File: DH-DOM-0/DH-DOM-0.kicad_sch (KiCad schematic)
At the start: 30 parts, among them J1 USB_C_Receptacle_USB2.0_14P, SW1 RST, SW2 BOOT, U1 MMC5983MA, U2 LSM6DSOXTR, U3 ESP32-S3-WROOM-1, U4 NCP1117-3.3_SOT223, U5 TVS1400DRV, U7 ST7789

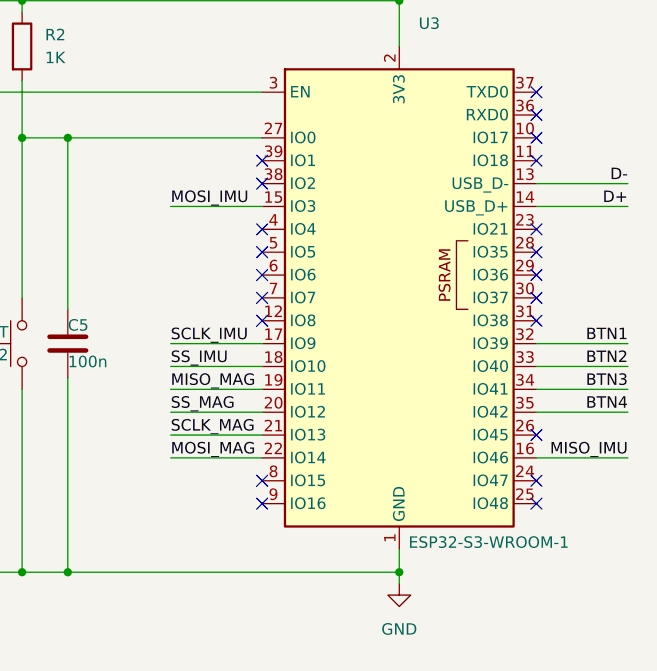
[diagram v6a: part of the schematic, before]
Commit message: edit
pcb almost done, last decoupling capacitors and screen routing left. also needs drc check
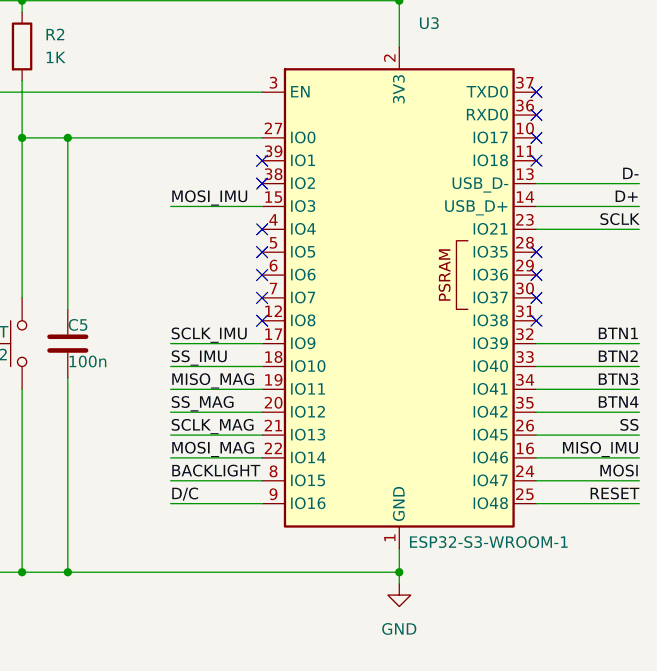
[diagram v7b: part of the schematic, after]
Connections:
- net BACKLIGHT: now also U3.8 (IO15)
- net D/C: now also U3.9 (IO16)
- net MOSI: now also U3.24 (IO47)
- net RESET: now also U3.25 (IO48)
- net SCLK: now also U3.23 (IO21)
- net SS: now also U3.26 (IO45)
- no-connect marks 27 -> 21
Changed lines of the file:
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@@
-	)
-	(no_connect
-		(at 154.94 116.84)
-	)
-	(no_connect
-		(at 185.42 116.84)
 	)
 	(no_connect
@@
 	)
 	(no_connect
-		(at 185.42 86.36)
-	)
-	(no_connect
 		(at 97.79 30.48)
 	)
@@
 	)
 	(no_connect
-		(at 185.42 109.22)
-	)
-	(no_connect
 		(at 154.94 93.98)
 	)
@@
 	)
 	(no_connect
-		(at 185.42 114.3)
-	)
-	(no_connect
 		(at 154.94 81.28)
-	)
-	(no_connect
-		(at 154.94 114.3)
 	)
 	(no_connect
@@
 	(wire
 		(pts
+			(xy 185.42 106.68) (xy 196.85 106.68)
+		)
+		(stroke
+			(width 0)
+			(type default)
+		)
+	)
+	(wire
+		(pts
 			(xy 41.91 45.72) (xy 41.91 49.53)
 		)
@@
 	(wire
 		(pts
-			(xy 185.42 101.6) (xy 195.58 101.6)
-		)
-		(stroke
-			(width 0)
-			(type default)
-		)
-	)
-	(wire
-		(pts
 			(xy 39.37 157.48) (xy 43.18 157.48)
 		)
@@
 	(wire
 		(pts
-			(xy 185.42 111.76) (xy 195.58 111.76)
-		)
-		(stroke
-			(width 0)
-			(type default)
-		)
-	)
-	(wire
-		(pts
-			(xy 185.42 83.82) (xy 195.58 83.82)
+			(xy 185.42 116.84) (xy 196.85 116.84)
 		)
 		(stroke
@@
 	(wire
 		(pts
+			(xy 185.42 99.06) (xy 196.85 99.06)
+		)
+		(stroke
+			(width 0)
+			(type default)
+		)
+	)
+	(wire
+		(pts
 			(xy 107.95 49.53) (xy 113.03 49.53)
 		)
@@
 	(wire
 		(pts
-			(xy 185.42 99.06) (xy 195.58 99.06)
-		)
-		(stroke
-			(width 0)
-			(type default)
-		)
-	)
-	(wire
-		(pts
 			(xy 63.5 68.58) (xy 69.85 68.58)
 		)
@@
 	(wire
 		(pts
+			(xy 185.42 104.14) (xy 196.85 104.14)
+		)
+		(stroke
+			(width 0)
+			(type default)
+		)
+	)
+	(wire
+		(pts
 			(xy 128.27 69.85) (xy 128.27 76.2)
 		)
@@
 	(wire
 		(pts
-			(xy 185.42 104.14) (xy 195.58 104.14)
-		)
-		(stroke
-			(width 0)
-			(type default)
-		)
-	)
-	(wire
-		(pts
 			(xy 39.37 19.05) (xy 41.91 19.05)
 		)
@@
 	(wire
 		(pts
+			(xy 185.42 81.28) (xy 196.85 81.28)
+		)
+		(stroke
+			(width 0)
+			(type default)
+		)
+	)
+	(wire
+		(pts
 			(xy 128.27 104.14) (xy 128.27 124.46)
 		)
@@
 	(wire
 		(pts
+			(xy 185.42 83.82) (xy 196.85 83.82)
+		)
+		(stroke
+			(width 0)
+			(type default)
+		)
+	)
+	(wire
+		(pts
 			(xy 113.03 16.51) (xy 113.03 19.05)
 		)
@@
 	(wire
 		(pts
-			(xy 185.42 106.68) (xy 195.58 106.68)
-		)
-		(stroke
-			(width 0)
-			(type default)
-		)
-	)
-	(wire
-		(pts
 			(xy 87.63 106.68) (xy 91.44 106.68)
 		)
@@
 	(wire
 		(pts
+			(xy 185.42 86.36) (xy 196.85 86.36)
+		)
+		(stroke
+			(width 0)
+			(type default)
+		)
+	)
+	(wire
+		(pts
 			(xy 15.24 133.35) (xy 15.24 138.43)
 		)
@@
 	(wire
 		(pts
+			(xy 185.42 109.22) (xy 196.85 109.22)
+		)
+		(stroke
+			(width 0)
+			(type default)
+		)
+	)
+	(wire
+		(pts
 			(xy 101.6 19.05) (xy 101.6 30.48)
 		)
@@
 	(wire
 		(pts
+			(xy 144.78 116.84) (xy 154.94 116.84)
+		)
+		(stroke
+			(width 0)
+			(type default)
+		)
+	)
+	(wire
+		(pts
 			(xy 81.28 45.72) (xy 81.28 49.53)
 		)
@@
 	(wire
 		(pts
+			(xy 144.78 114.3) (xy 154.94 114.3)
+		)
+		(stroke
+			(width 0)
+			(type default)
+		)
+	)
+	(wire
+		(pts
+			(xy 185.42 111.76) (xy 196.85 111.76)
+		)
+		(stroke
+			(width 0)
+			(type default)
+		)
+	)
+	(wire
+		(pts
 			(xy 73.66 157.48) (xy 77.47 157.48)
 		)
@@
 	(wire
 		(pts
-			(xy 185.42 81.28) (xy 195.58 81.28)
-		)
-		(stroke
-			(width 0)
-			(type default)
-		)
-	)
-	(wire
-		(pts
 			(xy 91.44 106.68) (xy 91.44 107.95)
 		)
@@
 	(wire
 		(pts
+			(xy 185.42 101.6) (xy 196.85 101.6)
+		)
+		(stroke
+			(width 0)
+			(type default)
+		)
+	)
+	(wire
+		(pts
 			(xy 110.49 60.96) (xy 128.27 60.96)
 		)
@@
 	(wire
 		(pts
+			(xy 185.42 114.3) (xy 196.85 114.3)
+		)
+		(stroke
+			(width 0)
+			(type default)
+		)
+	)
+	(wire
+		(pts
 			(xy 45.72 73.66) (xy 45.72 76.2)
 		)
@@
 	)
 	(label "D+"
-		(at 195.58 83.82 180)
+		(at 196.85 83.82 180)
 		(effects
 			(font
@@
 		)
 	)
+	(label "SCLK"
+		(at 196.85 86.36 180)
+		(effects
+			(font
+				(size 1.27 1.27)
+			)
+			(justify right bottom)
+		)
+	)
+	(label "RESET"
+		(at 196.85 116.84 180)
+		(effects
+			(font
+				(size 1.27 1.27)
+			)
+			(justify right bottom)
+		)
+	)
 	(label "D+"
 		(at 49.53 86.36 180)
@@
 	)
 	(label "BTN4"
-		(at 195.58 106.68 180)
+		(at 196.85 106.68 180)
 		(effects
 			(font
@@
 	)
 	(label "BTN1"
-		(at 195.58 99.06 180)
+		(at 196.85 99.06 180)
 		(effects
 			(font
@@
 	)
 	(label "MISO_IMU"
-		(at 195.58 111.76 180)
+		(at 196.85 111.76 180)
 		(effects
 			(font
@@
 	)
 	(label "BTN2"
-		(at 195.58 101.6 180)
+		(at 196.85 101.6 180)
 		(effects
 			(font
@@
 	)
 	(label "BTN3"
-		(at 195.58 104.14 180)
+		(at 196.85 104.14 180)
 		(effects
 			(font
@@
 	)
 	(label "D-"
-		(at 195.58 81.28 180)
+		(at 196.85 81.28 180)
+		(effects
+			(font
+				(size 1.27 1.27)
+			)
+			(justify right bottom)
+		)
+	)
+	(label "MOSI"
+		(at 196.85 114.3 180)
+		(effects
+			(font
+				(size 1.27 1.27)
+			)
+			(justify right bottom)
+		)
+	)
+	(label "SS"
+		(at 196.85 109.22 180)
 		(effects
 			(font
@@
 		)
 	)
+	(label "BACKLIGHT"
+		(at 144.78 114.3 0)
+		(effects
+			(font
+				(size 1.27 1.27)
+			)
+			(justify left bottom)
+		)
+	)
 	(label "MOSI_IMU"
 		(at 55.88 30.48 0)
@@
 		)
 	)
+	(label "D{slash}C"
+		(at 144.78 116.84 0)
+		(effects
+			(font
+				(size 1.27 1.27)
+			)
+			(justify left bottom)
+		)
+	)
